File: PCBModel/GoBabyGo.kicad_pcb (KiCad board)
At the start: 2 copper layers, 27 parts, among them J1 Conn_01x02_Pin, Q1 Q_NPN_BCE, Q2 Q_NPN_BCE, U1 NE555P, U2 NE555P

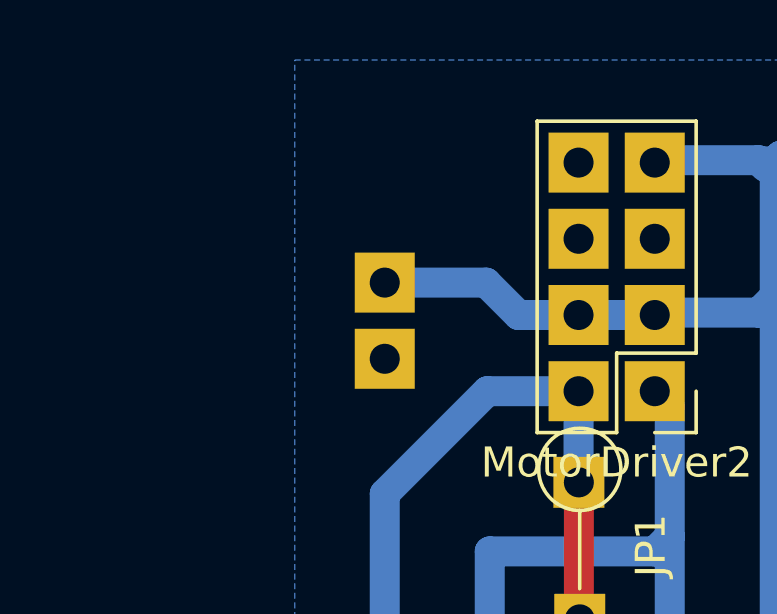
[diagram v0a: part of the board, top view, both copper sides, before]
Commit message: Minor PCB Model Fix
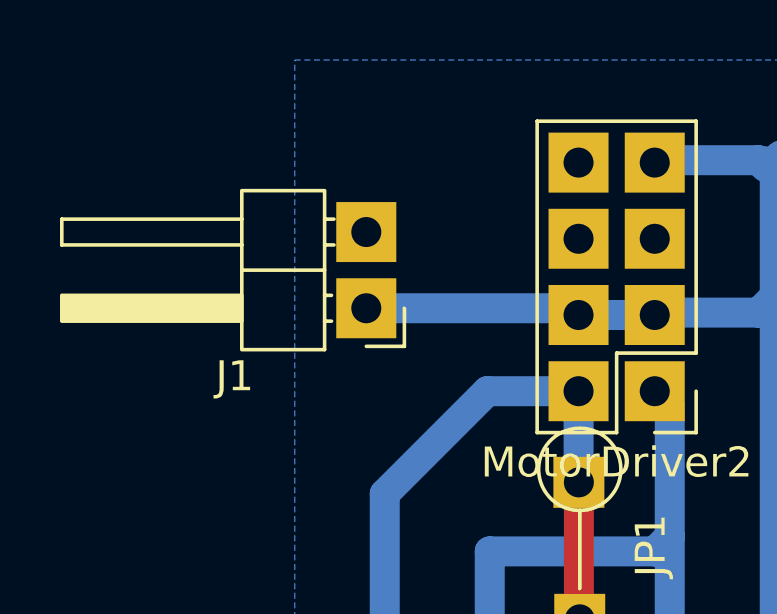
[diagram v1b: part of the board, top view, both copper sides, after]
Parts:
- J1: moved to F.Cu
- moved J1 1.05 mm to (109.9, 83.3)

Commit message: PCB review.
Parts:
- added JP5: Jumper_GND, Resistor_THT:R_Axial_DIN0207_L6.3mm_D2.5mm_P5.08mm_Vertical, F.Cu at (123.8, 109.8)
- Q1, Q2: value Q_NPN_BCE -> NPN
- moved Q1 8.17 mm to (152.3, 94.6)
- moved Q2 8.09 mm to (152.6, 91.3)
- moved C2 8.08 mm to (182.6, 85.2)
- moved C4 4.14 mm to (179.8, 103.8), turned to 90 degrees
- moved JP3 3.46 mm to (181.9, 91.8)
- moved JP2 2.95 mm to (183.3, 98.8)
- moved R13 1.27 mm to (184.1, 106.5)
- moved JP4 1.24 mm to (189.5, 114.0)
- moved U2 0.51 mm to (164.5, 98.5)
- turned C1 to -90 degrees
- turned C3 to 90 degrees
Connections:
- Q1 pad 1: Net-(Q1-B) -> Net-(Q1-C)
- Q1 pad 2: Net-(Q1-C) -> Net-(Q1-B)
- Q2 pad 1: Net-(Q2-B) -> Net-(Q2-C)
- Q2 pad 2: Net-(Q2-C) -> Net-(Q2-B)
- R12 pad 2: Net-(Q2-B) -> Net-(Q1-B)
- R14 pad 1: Net-(Q2-C) -> Net-(Q1-C)
- R3 pad 2: Net-(Q1-B) -> Net-(Q2-B)
- R4 pad 1: Net-(Q1-C) -> Net-(Q2-C)
- U1 pad 2: Net-(Q1-C) -> Net-(Q2-C)
- U2 pad 2: Net-(Q2-C) -> Net-(Q1-C)
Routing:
- net Net-(C3-Pad2): track 7.37 -> 18.0 mm
- net Net-(C1-Pad2): track 7.44 -> 18.0 mm
- net GND: track 0.00 -> 8.08 mm
- net +5V: track 251.6 -> 259.1 mm
- net Net-(U2-DISCH): track 11.0 -> 15.6 mm
- net Net-(U1-DISCH): track 16.4 -> 18.7 mm
- net Net-(Q1-C): track 13.2 -> 15.2 mm
- net /L_o: track 105.1 -> 103.2 mm
- net Net-(Q2-B): track 7.36 -> 8.84 mm
- net /R_o: track 94.2 -> 92.8 mm
- net Net-(Q1-B): track 7.80 -> 9.05 mm
- net Net-(Q2-C): track 13.4 -> 14.7 mm
- net /R: track 39.1 -> 39.9 mm
- net /L: track 56.8 -> 57.5 mm
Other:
- board outline added: 90 x 45.1 mm
